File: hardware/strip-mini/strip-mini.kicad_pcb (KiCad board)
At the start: 4 copper layers, 37.8 x 12 mm, 36 parts, among them J101 CORTEX-DEBUG, J102 JAE_DX07S016JA3, SW101 SW_Push, U101 AP2112K-3.3, U102 ATSAMD51G, U201 74AHC1G125, Y101 32k768

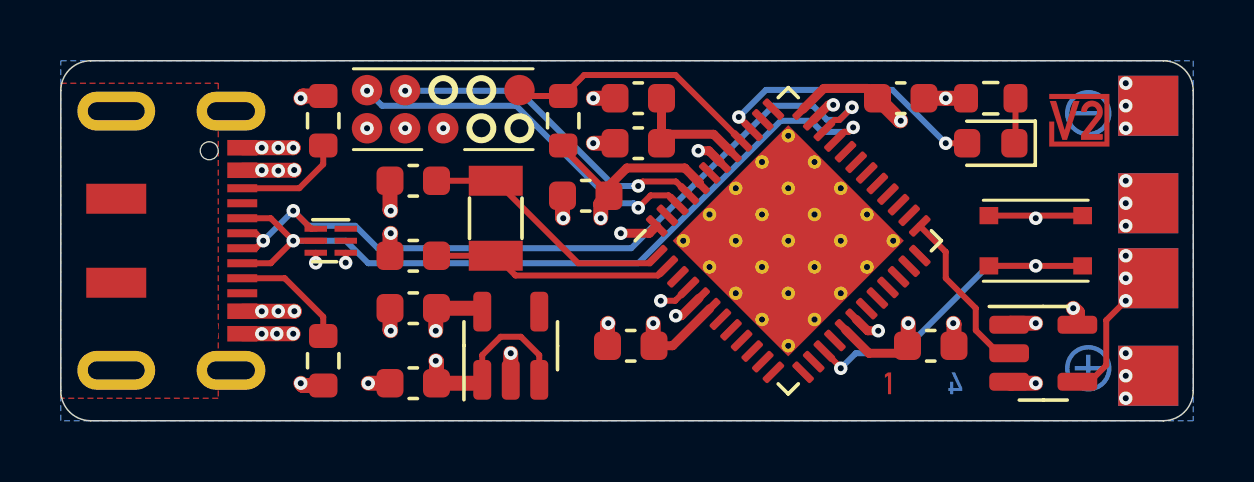
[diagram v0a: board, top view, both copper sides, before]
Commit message: Replace Order_Number
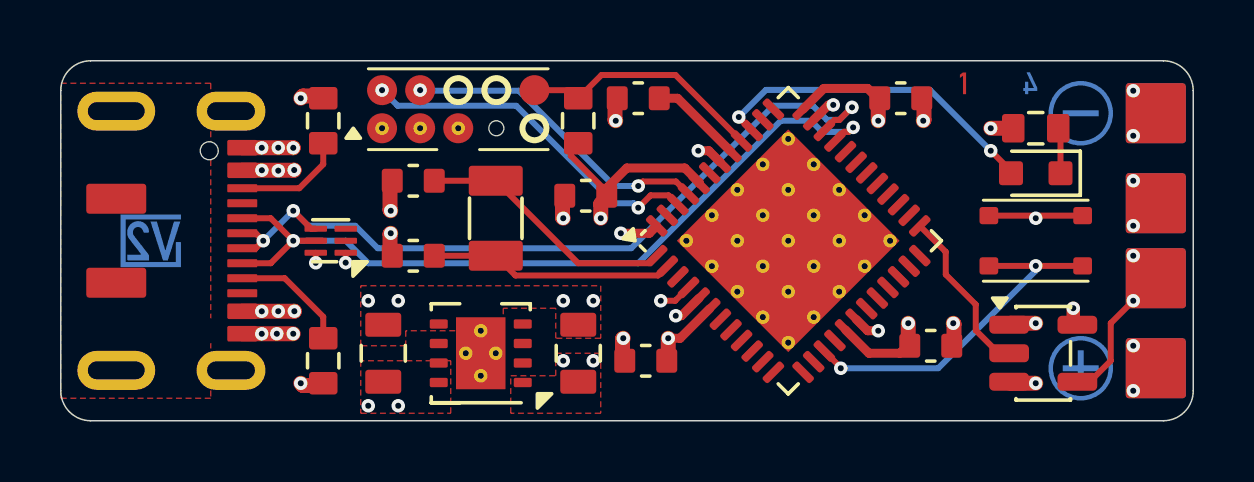
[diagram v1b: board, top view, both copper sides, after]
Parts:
- removed the C102 at (136.2, 105.8)
- removed the C107 at (128.8, 113.8)
- removed INFO102: ORDER-NUMBER, V2_Production:Order_Number
- removed the TP205 at (153.2, 107.8)
- removed the TP207 at (153.2, 104.5)
- removed the U101 at (132.0, 112.5)
- added C109: 10u, V2_Capacitor_SMD:C_0805, F.Cu at (134.2, 112.8)
- added TP206: ~, V2_TestPoint:TestPoint_Pad_2.0x2.0mm, F.Cu at (153.5, 107.8)
- added TP208: ~, V2_TestPoint:TestPoint_Pad_2.0x2.0mm, F.Cu at (153.5, 104.8)
- added U102: TPS78433QWDRBRQ1, V2_Package_SON:VSON-8-1_3x3mm_P0.65_EP1.65x2.4mm, F.Cu at (131.0, 112.8)
- C101: renamed from C109; footprint Capacitor_SMD:C_0603_1608Metric -> V2_Capacitor_SMD:C_0603
- C102: renamed from C110; footprint Capacitor_SMD:C_0603_1608Metric -> V2_Capacitor_SMD:C_0603
- C103: renamed from C101; footprint Capacitor_SMD:C_0603_1608Metric -> V2_Capacitor_SMD:C_0603
- C104: renamed from C103; footprint Capacitor_SMD:C_0603_1608Metric -> V2_Capacitor_SMD:C_0603
- C105: renamed from C104; footprint Capacitor_SMD:C_0603_1608Metric -> V2_Capacitor_SMD:C_0603
- C106: renamed from C105; footprint Capacitor_SMD:C_0603_1608Metric -> V2_Capacitor_SMD:C_0603
- C107: renamed from C106; footprint Capacitor_SMD:C_0603_1608Metric -> V2_Capacitor_SMD:C_0603
- C108: footprint Capacitor_SMD:C_0603_1608Metric -> V2_Capacitor_SMD:C_0805
- D101: footprint LED_SMD:LED_0603_1608Metric -> V2_LED:LED_0603
- ICON101: renamed from ICON102; moved to B.Cu
- J101: value CORTEX-DEBUG -> Cortex; footprint V2_Cortex_Debug:Cortex_Debug_Pad -> V2_Connector_Debug:Cortex
- J102: value JAE_DX07S016JA3 -> DX07S016JA3
- R101: renamed from R104; footprint Resistor_SMD:R_0603_1608Metric -> V2_Resistor_SMD:R_0603
- R102: renamed from R101; footprint Resistor_SMD:R_0603_1608Metric -> V2_Resistor_SMD:R_0603
- R103: renamed from R102; footprint Resistor_SMD:R_0603_1608Metric -> V2_Resistor_SMD:R_0603
- R104: renamed from R103; footprint Resistor_SMD:R_0603_1608Metric -> V2_Resistor_SMD:R_0603
- SW101: value SW_Push -> SKSG
- TP201, TP202, TP203, TP204: value TestPoint_Small -> ~
- TP205: renamed from TP206; value TestPoint_Small -> ~
- TP207: renamed from TP208; value TestPoint_Small -> ~
- U201: footprint Package_TO_SOT_SMD:SOT-23-5 -> V2_Package_TO_SOT_SMD:SOT-23-5
- moved ICON101 31.3 mm to (120.0, 109.0), turned to 180 degrees
- moved INFO101 10.3 mm to (148.2, 103.8)
- moved C108 1.80 mm to (127.8, 112.8), turned to 90 degrees
- moved D101 1.80 mm to (149.5, 106.8)
- moved R102 1.80 mm to (149.5, 105.2)
- moved C107 0.71 mm to (136.5, 113.0)
- moved J101 0.50 mm to (130.2, 105.2)
- moved R101 0.50 mm to (134.2, 105.0)
- moved TP201 0.35 mm to (153.5, 113.2)
- moved TP202 0.35 mm to (153.5, 113.2)
- moved TP207 0.35 mm to (153.5, 104.8)
- moved ICON102 0.25 mm to (151.0, 104.8)
- moved ICON103 0.25 mm to (151.0, 113.2)
- moved TP203 0.25 mm to (153.5, 110.2)
- moved TP204 0.25 mm to (153.5, 110.2)
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- renumbered ICON101 to ICON102, U102 to U101
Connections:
- net Earth renamed Shield
- C108 pad 1: +3V3 -> +5V
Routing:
- net +5V: track 10.8 -> 4.41 mm
- net +3V3: track 20.7 -> 17.5 mm
- net GND: track 24.5 -> 21.5 mm, vias 36 -> 33
- net /LED-onboard: track 9.35 -> 11.3 mm
- net /VDDCORE: track 4.18 -> 3.05 mm
- net /RESET: track 8.69 -> 8.03 mm
- net /LED Strip/WS2812-data: track 3.61 -> 3.71 mm, vias 3 -> 2
- added copper zone on F.Cu, net +3V3
- added copper zone on F.Cu, net +5V
- added copper zone on F.Cu, net GND
- added copper zone on In2.Cu, net GND
- removed copper zone on B.Cu, net GND

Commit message: Update
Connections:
- net Shield renamed /Shield
